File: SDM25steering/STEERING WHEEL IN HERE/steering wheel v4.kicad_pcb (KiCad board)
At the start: 4 copper layers, 162.2 x 126.4 mm, 82 parts, among them J1 Conn_01x04_Socket, J2 Conn_01x02, J3 Conn_01x02, J4 USB_B_Micro, J5 Conn_ARM_SWD_TagConnect_TC2030, U3 SN65HVD230, U5 USBLC6-2SC6, U6 MIC37100-3.3WS

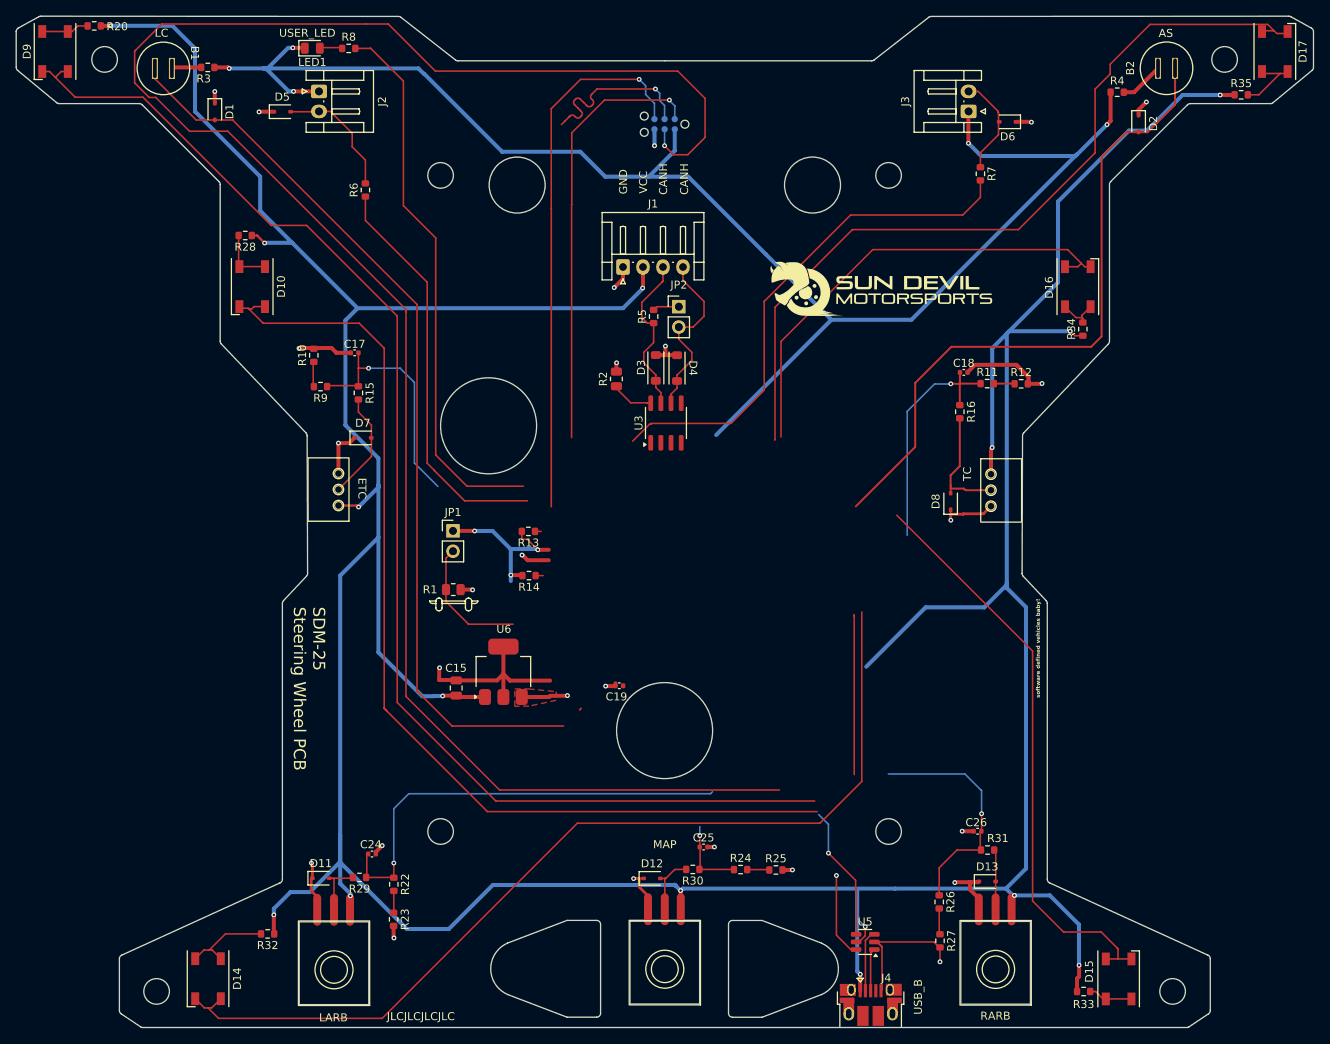
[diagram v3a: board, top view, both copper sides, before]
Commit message: Steering Wheel REV2
Complete overhaul of the steering wheel module complete - ready for review.
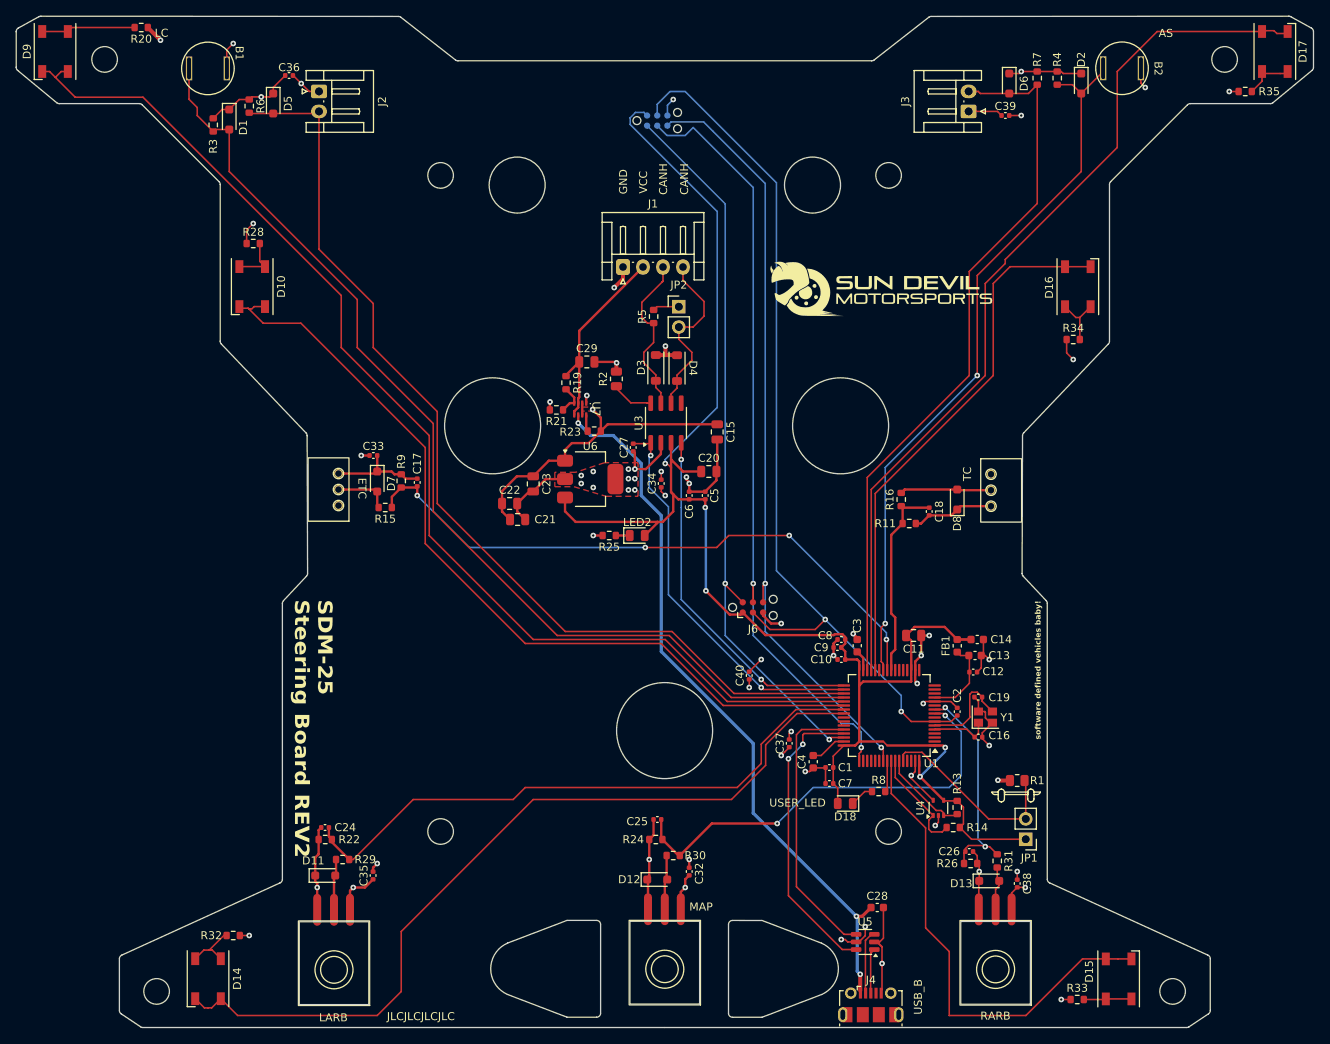
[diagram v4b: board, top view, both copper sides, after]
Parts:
- removed LED1: GREEN, LED_SMD:LED_0805_2012Metric
- removed R10, R12, R27: 1k, Resistor_SMD:R_0603_1608Metric
- added C1: 100nF, Capacitor_SMD:C_0402_1005Metric, F.Cu at (172.5, 119.5)
- added C10: 100nF, Capacitor_SMD:C_0402_1005Metric, F.Cu at (174.0, 106.0)
- added C11: 10uF, Capacitor_SMD:C_0805_2012Metric, F.Cu at (183.1, 103.0)
- added C12: 100nF, Capacitor_SMD:C_0402_1005Metric, F.Cu at (190.5, 107.6)
- added C13: 1uF, Capacitor_SMD:C_0603_1608Metric, F.Cu at (190.7, 105.5)
- added C14: 1uF, Capacitor_SMD:C_0603_1608Metric, F.Cu at (191.0, 103.5)
- added C16: 10pF, Capacitor_SMD:C_0402_1005Metric, F.Cu at (191.2, 115.7)
- added C2: 100nF, Capacitor_SMD:C_0402_1005Metric, F.Cu at (188.5, 112.5)
- added C20: 10uF, Capacitor_SMD:C_0805_2012Metric, F.Cu at (157.4, 82.5)
- added C21: 10uF, Capacitor_SMD:C_0805_2012Metric, F.Cu at (133.6, 88.5)
- added C22: 10uF, Capacitor_SMD:C_0805_2012Metric, F.Cu at (132.6, 86.5)
- added C23: 10uF, Capacitor_SMD:C_0805_2012Metric, F.Cu at (135.5, 84.0)
- added C27: 100nF, Capacitor_SMD:C_0402_1005Metric, F.Cu at (148.0, 79.5)
- added C28: 1uF, Capacitor_SMD:C_0603_1608Metric, F.Cu at (178.5, 137.0)
- added C29: 10uF, Capacitor_SMD:C_0805_2012Metric, F.Cu at (142.2, 68.8)
- added C3: 2.2uF, Capacitor_SMD:C_0603_1608Metric, F.Cu at (176.0, 104.3)
- added C32: 100nF, Capacitor_SMD:C_0402_1005Metric, F.Cu at (155.0, 132.5)
- added C33: 100nF, Capacitor_SMD:C_0402_1005Metric, F.Cu at (115.5, 80.5)
- added C34: 100nF, Capacitor_SMD:C_0402_1005Metric, F.Cu at (151.5, 84.0)
- added C35: 100nF, Capacitor_SMD:C_0402_1005Metric, F.Cu at (115.5, 133.0)
- added C36: 100nF, Capacitor_SMD:C_0402_1005Metric, F.Cu at (105.0, 33.0)
- added C37: 100nF, Capacitor_SMD:C_0402_1005Metric, F.Cu at (167.5, 116.5)
- added C38: 100nF, Capacitor_SMD:C_0402_1005Metric, F.Cu at (196.0, 134.0)
- added C39: 100nF, Capacitor_SMD:C_0402_1005Metric, F.Cu at (194.5, 38.0)
- added C4: 2.2uF, Capacitor_SMD:C_0603_1608Metric, F.Cu at (170.5, 118.8)
- added C40: 100nF, Capacitor_SMD:C_0402_1005Metric, F.Cu at (162.5, 108.0)
- added C5: 100nF, Capacitor_SMD:C_0402_1005Metric, F.Cu at (157.0, 85.5)
- added C6: 100nF, Capacitor_SMD:C_0402_1005Metric, F.Cu at (155.0, 85.5)
- added C7: 100nF, Capacitor_SMD:C_0402_1005Metric, F.Cu at (172.5, 121.5)
- added C8: 100nF, Capacitor_SMD:C_0402_1005Metric, F.Cu at (174.0, 103.5)
- added C9: 100nF, Capacitor_SMD:C_0402_1005Metric, F.Cu at (173.5, 104.5)
- added D18: GREEN, LED_SMD:LED_0805_2012Metric, F.Cu at (174.5, 124.0)
- added FB1: 120R, Inductor_SMD:L_0603_1608Metric, F.Cu at (188.5, 104.3)
- added J6: Conn_ARM_SWD_TagConnect_TC2030, Connector:Tag-Connect_TC2030-IDC-NL_2x03_P1.27mm_Vertical, F.Cu at (163.0, 99.5)
- added LED2: RED, LED_SMD:LED_0805_2012Metric, F.Cu at (148.5, 90.5)
- added R19: 10k, Resistor_SMD:R_0603_1608Metric, F.Cu at (139.6, 71.4)
- added R21: 10k, Resistor_SMD:R_0603_1608Metric, F.Cu at (138.4, 74.8)
- added U1: STM32F405RGT6, Package_QFP:LQFP-64_10x10mm_P0.5mm, F.Cu at (180.0, 113.0)
- added U4: 24LC01BT-E/LT, Package_TO_SOT_SMD:SOT-353_SC-70-5, F.Cu at (186.2, 124.5)
- added U7: TPS2116, Library:SOT-5X3, F.Cu at (142.9, 74.7)
- added Y1: 12MHz, Crystal:Crystal_SMD_2520-4Pin_2.5x2.0mm, F.Cu at (192.0, 113.2)
- D1, D11, D12, D13, D2, D5, D6, D7, D8: footprint Diode_SMD:D_SOD-323 -> Diode_SMD:D_SOD-323_HandSoldering
- J4: footprint Connector_USB:USB_Micro-B_Amphenol_10103594-0001LF_Horizontal -> Connector_USB:USB_Micro-B_Molex-105017-0001
- JP2: value Bus Termination -> Bus Term.
- R11, R22, R24, R26, R9: value 1k -> 2k
- R23: value 1k -> 10k
- R25: value 1k -> 220
- R3, R6, R7: value 220 -> 10k
- moved R8 114.1 mm to (178.7, 122.5)
- moved JP1 81.3 mm to (197.1, 128.5), turned to 180 degrees
- moved R1 74.4 mm to (196.0, 121.1), turned to 0 degrees
- moved R23 66.0 mm to (143.1, 77.5), turned to 180 degrees
- moved R13 63.8 mm to (188.5, 124.5), turned to 90 degrees
- moved R14 61.7 mm to (188.0, 127.0), turned to 0 degrees
- moved R25 46.7 mm to (145.0, 90.5), turned to 180 degrees
- moved C15 45.7 mm to (158.5, 77.5), turned to -90 degrees
- moved C19 44.9 mm to (191.1, 110.7)
- moved U6 26.4 mm to (142.6, 83.5), turned to 0 degrees
- moved R11 20.0 mm to (182.5, 89.0)
- moved C17 18.0 mm to (121.0, 83.9), turned to 90 degrees
- moved C18 17.9 mm to (185.0, 87.5), turned to -90 degrees
- moved R6 17.9 mm to (100.0, 36.8), turned to -90 degrees
- moved R9 15.5 mm to (119.0, 83.7), turned to 90 degrees
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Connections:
- net /B3 renamed /SHIFT1
- net /B4 renamed /SHIFT2
- B1 pad 1: Net-(B1-Pin_1) -> VCC
- B2 pad 1: Net-(B2-Pin_1) -> VCC
- J1 pad 2: VCC -> +5VD
- J2 pad 1: +3.3V -> VCC
- J3 pad 1: +3.3V -> VCC
- J4 pad 1: VCC -> VBUS
- R11 pad 2: Net-(R11-Pad2) -> GND
- R13 pad 1: /I2C1_SCL -> /I2C1_SDA
- R14 pad 1: /I2C1_SDA -> /I2C1_SCL
- R22 pad 2: Net-(R22-Pad2) -> GND
- R23 pad 1: Net-(R22-Pad2) -> VCC
- R23 pad 2: GND -> Net-(U7-ST)
- R24 pad 2: Net-(R24-Pad2) -> GND
- R25 pad 1: Net-(R24-Pad2) -> Net-(LED2-K)
- R26 pad 2: Net-(R26-Pad2) -> GND
- R3 pad 1: +3.3V -> GND
- R3 pad 2: Net-(B1-Pin_1) -> /BUTTON_LC
- R4 pad 1: +3.3V -> GND
- R4 pad 2: Net-(B2-Pin_1) -> /BUTTON_AS
- R6 pad 1: /BUTTON3 -> GND
- R7 pad 1: /BUTTON4 -> GND
- R9 pad 2: Net-(R10-Pad1) -> GND
- U3 pad 1: /CRX -> /CTX
- U3 pad 4: /CTX -> /CRX
- U5 pad 4: /USB_D+ -> /USB_D-
- U5 pad 6: /USB_D- -> /USB_D+
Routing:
- net VCC: track 532.2 -> 89.7 mm, vias 15 -> 19
- net /NRST: track 239.8 -> 112.5 mm, vias 1 -> 2
- net /SHIFT1: track 15.8 -> 124.7 mm
- net VBUS: track 0.00 -> 90.5 mm, vias 0 -> 3
- net /SHIFT2: track 12.7 -> 91.1 mm
- net /SWCLK: track 22.3 -> 96.6 mm, vias 1 -> 2
- net GND: track 121.9 -> 193.5 mm, vias 25 -> 45
- net /BUTTON4: track 64.7 -> 0.00 mm
- net /USER_LED: track 68.6 -> 3.93 mm
- net /BUTTON3: track 51.0 -> 0.00 mm
- net /CTX: track 0.00 -> 49.1 mm, vias 0 -> 2
- net /AIN6: track 29.9 -> 77.9 mm, vias 1 -> 4
- net /AIN2: track 9.53 -> 54.6 mm, vias 1 -> 2
- net /CRX: track 0.00 -> 44.4 mm, vias 0 -> 2
- net /LED2: track 147.6 -> 105.4 mm
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- added copper zone on F.Cu, net GND
- added copper zone on F.Cu, net VCC
- added copper zone on In2.Cu, net VCC
- removed copper zone on F.Cu, net +3.3V
- removed copper zone on In2.Cu, net GND
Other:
- outline, holes or cut-outs redrawn
- board text added: "SDM-25 Steering Board REV2"
- board text added: "digital jesus take the wheel"
- board text removed: "SDM-25 Steering Wheel PCB"
